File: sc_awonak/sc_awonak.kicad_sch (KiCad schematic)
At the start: 41 parts, among them J1 Conn_01x02, J2 Conn_01x02, J3 Analog Input, J4 Digital Input, J5 Analog Output

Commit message: More revision updates and add preview image
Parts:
- added J6: Conn_01x02, Connector_PinHeader_2.54mm:PinHeader_1x02_P2.54mm_Horizontal, symbol Connector_Generic:Conn_01x02
- A1: value Arduino_Nano_Socket -> Arduino Nano
- C1, C2, C3, C4: value 0.1uF_0603_16V -> 0.1uF; Display 0.1uF -> (none); JLCPCB ID C14663 -> (none); Manufacturer AVX Corporation -> (none); Part Number 0603YC104KAT2A -> (none); Specifications 0.1uF, Min. 16V 10%, X7R or X5R or similar -> (none)
- C5: value 0.1uF_0603_16V -> 0.1uF; JLCPCB ID C14663 -> (none); Manufacturer AVX Corporation -> (none); Part Number 0603YC104KAT2A -> (none); Specifications 0.1uF, Min. 16V 10%, X7R or X5R or similar -> (none)
- C6: value 0.1uF_0603_16V -> 4.7uF; Display 4.7uF -> (none); JLCPCB ID C14663 -> (none); Manufacturer AVX Corporation -> (none); Part Number 0603YC104KAT2A -> (none); Specifications 0.1uF, Min. 16V 10%, X7R or X5R or similar -> (none)
- R11, R12, R13, R14: Display (none) -> RLED
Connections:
- net GND: now also J6.2 (Pin_2)
- net VIN: now reaches A1.VIN
- net VIN: now also J6.1 (Pin_1)
- no-connect marks 9 -> 8

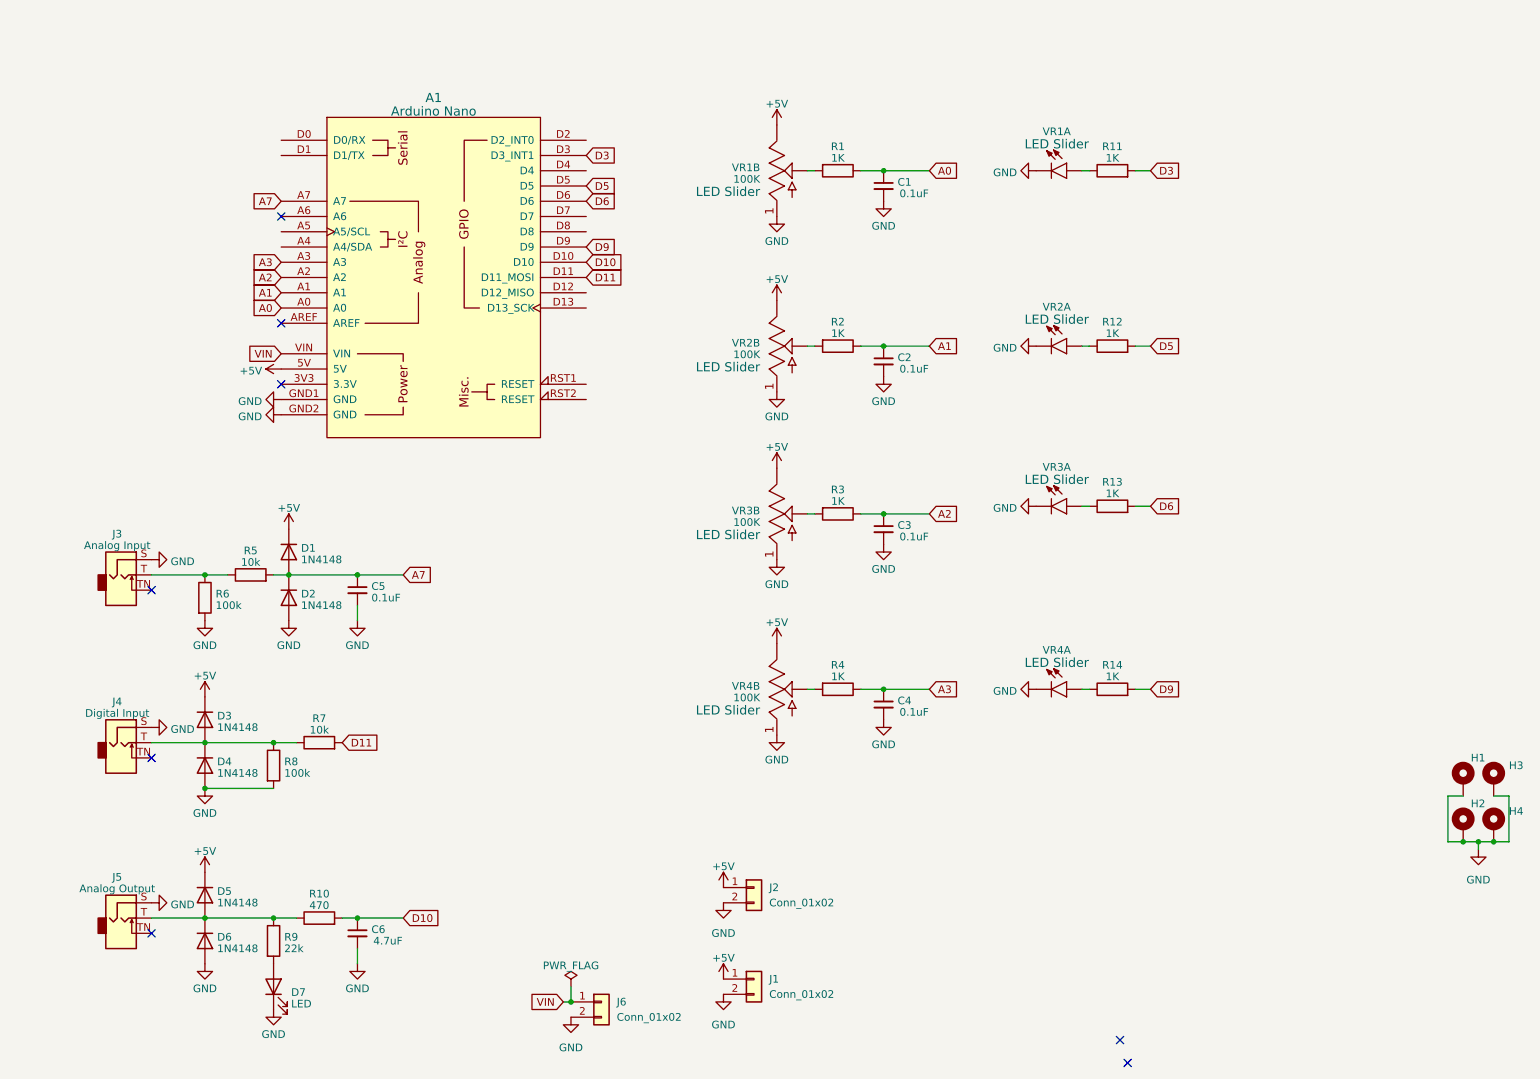
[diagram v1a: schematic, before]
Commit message: Added 3d rendering, schematic PDF, and more pcb revisions.
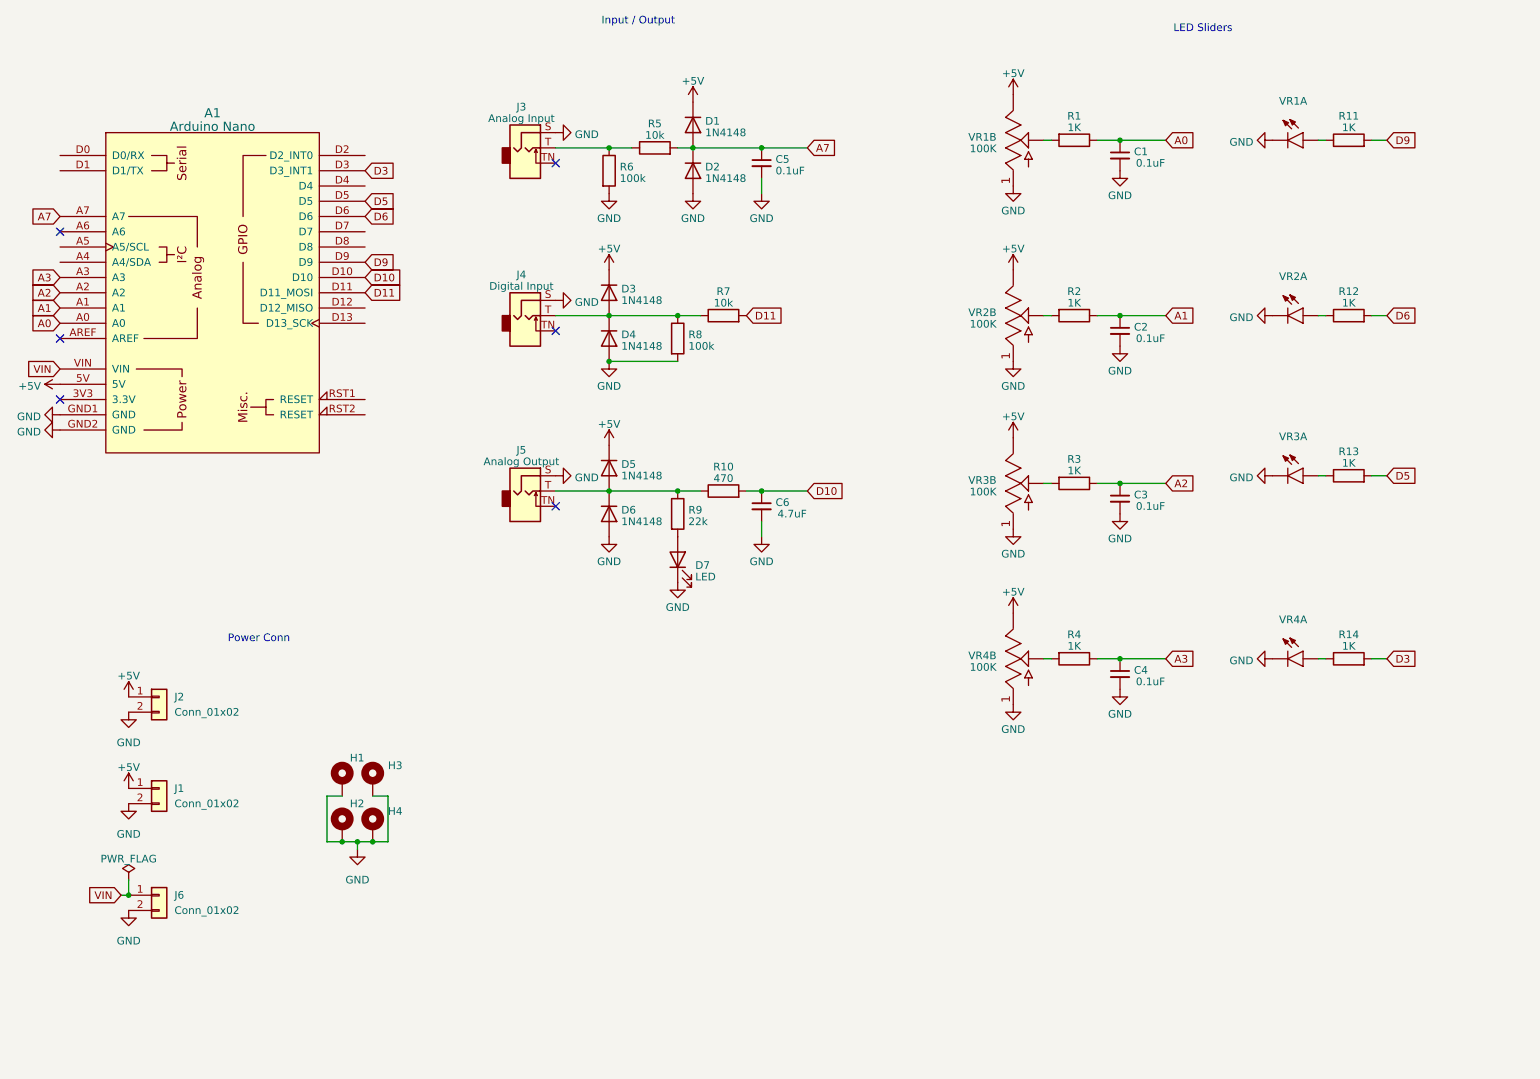
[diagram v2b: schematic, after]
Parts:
- VR1, VR2, VR3, VR4: Display LED Slider -> (none); Manufacturer Top-Up -> (none); Part Number PTL20-10O1-104B2 -> (none); Specifications B100K, No Detent, White LED, 15mm lever, 20mm tra -> (none)
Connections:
- net D3: now also R14.2; no longer R11.2
- net D5: now also R13.2; no longer R12.2
- net D6: now also R12.2; no longer R13.2
- net D9: now also R11.2; no longer R14.2
- no-connect marks 8 -> 6
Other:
- note added: "Input / Output"
- note added: "LED Sliders"
- note added: "Power Conn"
- title: (none) -> Synth Card - Adam Wonak
- moved on the sheet: A1, C1, C2, C3, C4, C5, C6, D1, D2, D3, D4, D5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

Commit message: Added BOM to README
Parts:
- D1, D2, D3, D4, D5, D6: value 1N4148 -> BAT43
- R11, R12, R13, R14: value 1K -> RLED
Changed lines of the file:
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@@
       (effects (font (size 1.27 1.27)) (justify left))
     )
-    (property "Value" "1N4148" (at 130.302 67.3173 90)
+    (property "Value" "BAT43" (at 130.302 67.3173 90)
       (effects (font (size 1.27 1.27)) (justify left))
     )
@@
       (effects (font (size 1.27 1.27)) (justify left))
     )
-    (property "Value" "1N4148" (at 144.272 39.3773 90)
+    (property "Value" "BAT43" (at 144.272 39.3773 90)
       (effects (font (size 1.27 1.27)) (justify left))
     )
@@
       (effects (font (size 1.27 1.27)) (justify left))
     )
-    (property "Value" "1N4148" (at 130.302 104.1473 90)
+    (property "Value" "BAT43" (at 130.302 104.1473 90)
       (effects (font (size 1.27 1.27)) (justify left))
     )
@@
       (effects (font (size 1.27 1.27)) (justify left))
     )
-    (property "Value" "1N4148" (at 144.272 46.9973 90)
+    (property "Value" "BAT43" (at 144.272 46.9973 90)
       (effects (font (size 1.27 1.27)) (justify left))
     )
@@
       (effects (font (size 1.27 1.27)) (justify left))
     )
-    (property "Value" "1N4148" (at 130.302 74.9373 90)
+    (property "Value" "BAT43" (at 130.302 74.9373 90)
       (effects (font (size 1.27 1.27)) (justify left))
     )
@@
       (effects (font (size 1.27 1.27)))
     )
-    (property "Value" "1K" (at 251.46 124.8951 90)
+    (property "Value" "RLED" (at 251.46 124.8951 90)
       (effects (font (size 1.27 1.27)))
     )
@@
       (effects (font (size 1.27 1.27)))
     )
-    (property "Value" "1K" (at 251.46 94.4151 90)
+    (property "Value" "RLED" (at 251.46 94.4151 90)
       (effects (font (size 1.27 1.27)))
     )
@@
       (effects (font (size 1.27 1.27)))
     )
-    (property "Value" "1K" (at 251.46 67.7451 90)
+    (property "Value" "RLED" (at 251.46 67.7451 90)
       (effects (font (size 1.27 1.27)))
     )
@@
       (effects (font (size 1.27 1.27)) (justify left))
     )
-    (property "Value" "1N4148" (at 130.302 96.5273 90)
+    (property "Value" "BAT43" (at 130.302 96.5273 90)
       (effects (font (size 1.27 1.27)) (justify left))
     )
@@
       (effects (font (size 1.27 1.27)))
     )
-    (property "Value" "1K" (at 251.46 38.5351 90)
-      (effects (font (size 1.27 1.27)))
-    )
+    (property "Value" "RLED" (at 251.46 38.5351 90)
+      (effects (font (size 1.27 1.27)))
+    )

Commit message: Add ibom and update gitignore
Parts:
- H1, H2, H3, H4, J6: now left out of the parts list
- J4: renamed from J2; now left out of the parts list
- J5: renamed from J1; now left out of the parts list
- R11, R12, R13, R14: value RLED -> 1K
- renumbered J3 to J1, J4 to J2, J5 to J3
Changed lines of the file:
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@@
   )
   (symbol (lib_id "Mechanical:MountingHole_Pad") (at 88.9 147.32 0) (unit 1)
-    (in_bom yes) (on_board yes) (dnp no) (fields_autoplaced)
+    (in_bom no) (on_board yes) (dnp no) (fields_autoplaced)
     (property "Reference" "H3" (at 91.44 144.7799 0)
       (effects (font (size 1.27 1.27)) (justify left))
@@
   (symbol (lib_id "Connector_Audio:AudioJack2_SwitchT") (at 114.3 99.06 0) (unit 1)
     (in_bom yes) (on_board yes) (dnp no) (fields_autoplaced)
-    (property "Reference" "J5" (at 113.665 92.2401 0)
+    (property "Reference" "J3" (at 113.665 92.2401 0)
       (effects (font (size 1.27 1.27)))
     )
@@
       (project "sc_awonak"
         (path "/3202d24d-726e-4f07-84c0-3006af20163a"
-          (reference "J5") (unit 1)
+          (reference "J3") (unit 1)
         )
       )
@@
   )
   (symbol (lib_id "Connector_Generic:Conn_01x02") (at 53.34 133.35 0) (unit 1)
-    (in_bom yes) (on_board yes) (dnp no) (fields_autoplaced)
-    (property "Reference" "J2" (at 55.88 133.3499 0)
-      (effects (font (size 1.27 1.27)) (justify left))
-    )
-    (property "Value" "Conn_01x02" (at 55.88 135.8899 0)
+    (in_bom no) (on_board yes) (dnp no) (fields_autoplaced)
+    (property "Reference" "J4" (at 55.372 133.9763 0)
+      (effects (font (size 1.27 1.27)) (justify left))
+    )
+    (property "Value" "Conn_01x02" (at 55.372 135.8973 0)
       (effects (font (size 1.27 1.27)) (justify left))
     )
@@
       (project "sc_awonak"
         (path "/3202d24d-726e-4f07-84c0-3006af20163a"
-          (reference "J2") (unit 1)
+          (reference "J4") (unit 1)
         )
       )
@@
   )
   (symbol (lib_id "Mechanical:MountingHole_Pad") (at 83.82 154.94 0) (unit 1)
-    (in_bom yes) (on_board yes) (dnp no)
+    (in_bom no) (on_board yes) (dnp no)
     (property "Reference" "H2" (at 85.09 151.13 0)
       (effects (font (size 1.27 1.27)) (justify left))
@@
   (symbol (lib_id "Connector_Audio:AudioJack2_SwitchT") (at 114.3 41.91 0) (unit 1)
     (in_bom yes) (on_board yes) (dnp no) (fields_autoplaced)
-    (property "Reference" "J3" (at 113.665 35.0901 0)
+    (property "Reference" "J1" (at 113.665 35.0901 0)
       (effects (font (size 1.27 1.27)))
     )
@@
       (project "sc_awonak"
         (path "/3202d24d-726e-4f07-84c0-3006af20163a"
-          (reference "J3") (unit 1)
+          (reference "J1") (unit 1)
         )
       )
@@
   (symbol (lib_id "Connector_Audio:AudioJack2_SwitchT") (at 114.3 69.85 0) (unit 1)
     (in_bom yes) (on_board yes) (dnp no) (fields_autoplaced)
-    (property "Reference" "J4" (at 113.665 63.0301 0)
+    (property "Reference" "J2" (at 113.665 63.0301 0)
       (effects (font (size 1.27 1.27)))
     )
@@
       (project "sc_awonak"
         (path "/3202d24d-726e-4f07-84c0-3006af20163a"
-          (reference "J4") (unit 1)
+          (reference "J2") (unit 1)
         )
       )
@@
       (effects (font (size 1.27 1.27)))
     )
-    (property "Value" "RLED" (at 251.46 124.8951 90)
+    (property "Value" "1K" (at 251.46 124.8951 90)
       (effects (font (size 1.27 1.27)))
     )
@@
   )
   (symbol (lib_id "Connector_Generic:Conn_01x02") (at 53.34 148.59 0) (unit 1)
-    (in_bom yes) (on_board yes) (dnp no) (fields_autoplaced)
-    (property "Reference" "J1" (at 55.88 148.5899 0)
-      (effects (font (size 1.27 1.27)) (justify left))
-    )
-    (property "Value" "Conn_01x02" (at 55.88 151.1299 0)
+    (in_bom no) (on_board yes) (dnp no) (fields_autoplaced)
+    (property "Reference" "J5" (at 55.372 149.2163 0)
+      (effects (font (size 1.27 1.27)) (justify left))
+    )
+    (property "Value" "Conn_01x02" (at 55.372 151.1373 0)
       (effects (font (size 1.27 1.27)) (justify left))
     )
@@
       (project "sc_awonak"
         (path "/3202d24d-726e-4f07-84c0-3006af20163a"
-          (reference "J1") (unit 1)
+          (reference "J5") (unit 1)
         )
       )
@@
   )
   (symbol (lib_id "Mechanical:MountingHole_Pad") (at 88.9 154.94 0) (unit 1)
-    (in_bom yes) (on_board yes) (dnp no) (fields_autoplaced)
+    (in_bom no) (on_board yes) (dnp no) (fields_autoplaced)
     (property "Reference" "H4" (at 91.44 152.3999 0)
       (effects (font (size 1.27 1.27)) (justify left))
@@
   )
   (symbol (lib_id "Connector_Generic:Conn_01x02") (at 53.34 166.37 0) (unit 1)
-    (in_bom yes) (on_board yes) (dnp no) (fields_autoplaced)
-    (property "Reference" "J6" (at 55.88 166.3699 0)
-      (effects (font (size 1.27 1.27)) (justify left))
-    )
-    (property "Value" "Conn_01x02" (at 55.88 168.9099 0)
+    (in_bom no) (on_board yes) (dnp no) (fields_autoplaced)
+    (property "Reference" "J6" (at 55.372 166.9963 0)
+      (effects (font (size 1.27 1.27)) (justify left))
+    )
+    (property "Value" "Conn_01x02" (at 55.372 168.9173 0)
       (effects (font (size 1.27 1.27)) (justify left))
     )
@@
   )
   (symbol (lib_id "Mechanical:MountingHole_Pad") (at 83.82 147.32 0) (unit 1)
-    (in_bom yes) (on_board yes) (dnp no)
+    (in_bom no) (on_board yes) (dnp no)
     (property "Reference" "H1" (at 85.09 143.51 0)
       (effects (font (size 1.27 1.27)) (justify left))
@@
       (effects (font (size 1.27 1.27)))
     )
-    (property "Value" "RLED" (at 251.46 94.4151 90)
+    (property "Value" "1K" (at 251.46 94.4151 90)
       (effects (font (size 1.27 1.27)))
     )
@@
       (effects (font (size 1.27 1.27)))
     )
-    (property "Value" "RLED" (at 251.46 67.7451 90)
+    (property "Value" "1K" (at 251.46 67.7451 90)
       (effects (font (size 1.27 1.27)))
     )
@@
       (effects (font (size 1.27 1.27)))
     )
-    (property "Value" "RLED" (at 251.46 38.5351 90)
-      (effects (font (size 1.27 1.27)))
-    )
+    (property "Value" "1K" (at 251.46 38.5351 90)
+      (effects (font (size 1.27 1.27)))
+    )

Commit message: hardware revision ver0.2
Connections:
- net D10: now also D5.2 (A), D6.1 (K), R10.1, R9.1; no longer C6.1, R10.2
- new net: C6.1, J3.T, R10.2
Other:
- moved on the sheet: C6, D5, D6, D7, J3, R10, R9
